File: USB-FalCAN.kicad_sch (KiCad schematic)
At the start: 58 parts, among them J1 Conn_01x17_Pin, J10 CAN, J2 NC, J3 Conn_01x17_Pin, J4 USB2.0_16P, J5 Boot, J6 NC, J7 DE9_Receptacle, J8 RS-485/422-TX, J9 RS-422-RX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

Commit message: Replace USB-TouCAN files with USB-FalCAN
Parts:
- J7: footprint Connector_Dsub:DSUB-9_Pins_Horizontal_P2.77x2.84mm_EdgePinOffset7.70mm_Housed_MountingHolesOffset9.12mm -> Connector_Dsub:DSUB-9_Female_Horizontal_P2.77x2.84mm_EdgePinOffset7.70mm_Housed_MountingHolesOffset9.12mm
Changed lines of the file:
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@@
 	(title_block
 		(title "FalCAN Probe")
-		(rev "1")
+		(rev "0")
 		(company "ABNielsen.com")
 	)
@@
 			)
 		)
-		(property "Footprint" "Connector_Dsub:DSUB-9_Pins_Horizontal_P2.77x2.84mm_EdgePinOffset7.70mm_Housed_MountingHolesOffset9.12mm"
+		(property "Footprint" "Connector_Dsub:DSUB-9_Female_Horizontal_P2.77x2.84mm_EdgePinOffset7.70mm_Housed_MountingHolesOffset9.12mm"
 			(at 161.29 170.18 0)
 			(effects

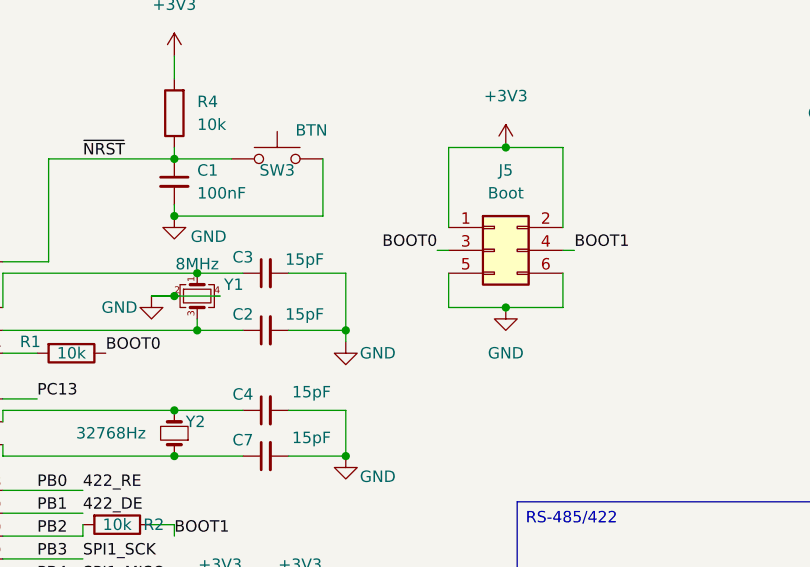
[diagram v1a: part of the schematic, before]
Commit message: Improve silk
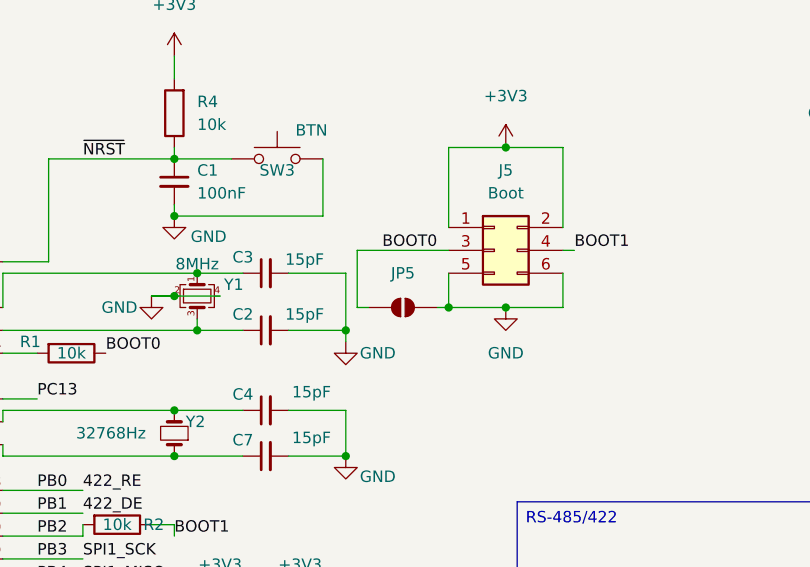
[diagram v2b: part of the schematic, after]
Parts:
- added JP5: SolderJumper_2_Open, Jumper:SolderJumper-2_P1.3mm_Open_RoundedPad1.0x1.5mm, symbol Jumper:SolderJumper_2_Open
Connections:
- net BOOT0: now also JP5.1 (A)
- net GND: now also JP5.2 (B)
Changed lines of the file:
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@@
 	(title_block
 		(title "FalCAN Probe")
-		(rev "0")
+		(rev "1")
 		(company "ABNielsen.com")
 	)
@@
 	)
 	(junction
+		(at 191.77 53.34)
+		(diameter 0)
+		(color 0 0 0 0)
+	)
+	(junction
 		(at 267.97 102.87)
 		(diameter 0)
@@
 	(wire
 		(pts
-			(xy 190.5 46.99) (xy 191.77 46.99)
-		)
-		(stroke
-			(width 0)
-			(type default)
-		)
-	)
-	(wire
-		(pts
 			(xy 76.2 24.13) (xy 82.55 24.13)
 		)
@@
 	(wire
 		(pts
+			(xy 181.61 53.34) (xy 182.88 53.34)
+		)
+		(stroke
+			(width 0)
+			(type default)
+		)
+	)
+	(wire
+		(pts
 			(xy 35.56 123.19) (xy 36.83 123.19)
 		)
@@
 	(wire
 		(pts
+			(xy 190.5 53.34) (xy 191.77 53.34)
+		)
+		(stroke
+			(width 0)
+			(type default)
+		)
+	)
+	(wire
+		(pts
 			(xy 50.8 78.74) (xy 50.8 81.28)
 		)
@@
 	(wire
 		(pts
+			(xy 181.61 46.99) (xy 191.77 46.99)
+		)
+		(stroke
+			(width 0)
+			(type default)
+		)
+	)
+	(wire
+		(pts
 			(xy 151.13 154.94) (xy 153.67 154.94)
 		)
@@
 	(wire
 		(pts
+			(xy 181.61 53.34) (xy 181.61 46.99)
+		)
+		(stroke
+			(width 0)
+			(type default)
+		)
+	)
+	(wire
+		(pts
 			(xy 262.89 144.78) (xy 267.97 144.78)
 		)
@@
 					(unit 1)
 				)
+			)
+		)
+	)
+	(symbol
+		(lib_id "Jumper:SolderJumper_2_Open")
+		(at 186.69 53.34 0)
+		(unit 1)
+		(exclude_from_sim no)
+		(in_bom no)
+		(on_board yes)
+		(dnp no)
+		(fields_autoplaced yes)
+		(property "Reference" "JP5"
+			(at 186.69 49.53 0)
+			(effects
+				(font
+					(size 1.27 1.27)
+				)
+			)
+		)
+		(property "Value" "SolderJumper_2_Open"
+			(at 186.69 49.53 0)
+			(effects
+				(font
+					(size 1.27 1.27)
+				)
+				(hide yes)
+			)
+		)
+		(property "Footprint" "Jumper:SolderJumper-2_P1.3mm_Open_RoundedPad1.0x1.5mm"
+			(at 186.69 53.34 0)
+			(effects
+				(font
+					(size 1.27 1.27)
+				)
+				(hide yes)
+			)
+		)
+		(property "Datasheet" "~"
+			(at 186.69 53.34 0)
+			(effects
+				(font
+					(size 1.27 1.27)
+				)
+				(hide yes)
+			)
+		)
+		(property "Description" "Solder Jumper, 2-pole, open"
+			(at 186.69 53.34 0)
+			(effects
+				(font
+					(size 1.27 1.27)
+				)
+				(hide yes)
+			)
+		)
+		(pin "2"
+		)
+		(pin "1"
+		)
+		(instances
+			(project "USB-FalCAN"
+				(path "/26096f25-a87e-4f6d-a99b-624957e9ad57"
+					(reference "JP5")
+					(unit 1)
+				)
